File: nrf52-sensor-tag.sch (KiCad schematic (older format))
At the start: 16 parts, among them IC2 VEML6030, IC3 MS860702BA01-50, J3 Conn_01x07_Male, U1 MS88SF2

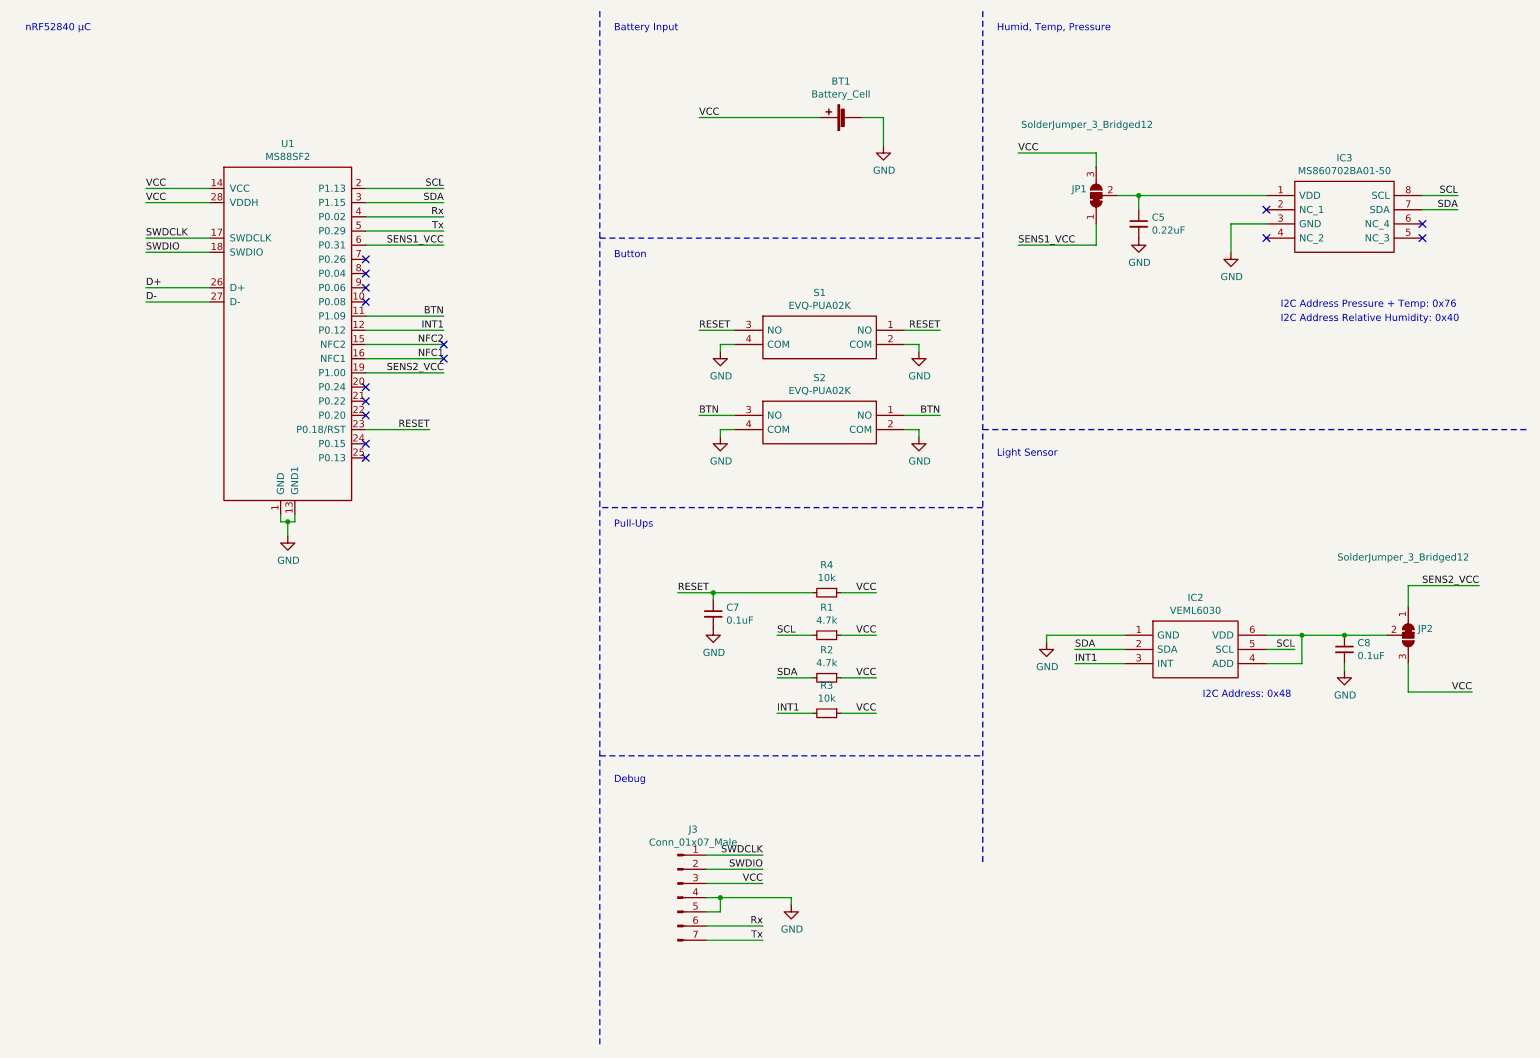
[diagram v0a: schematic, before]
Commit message: Add RGB LED
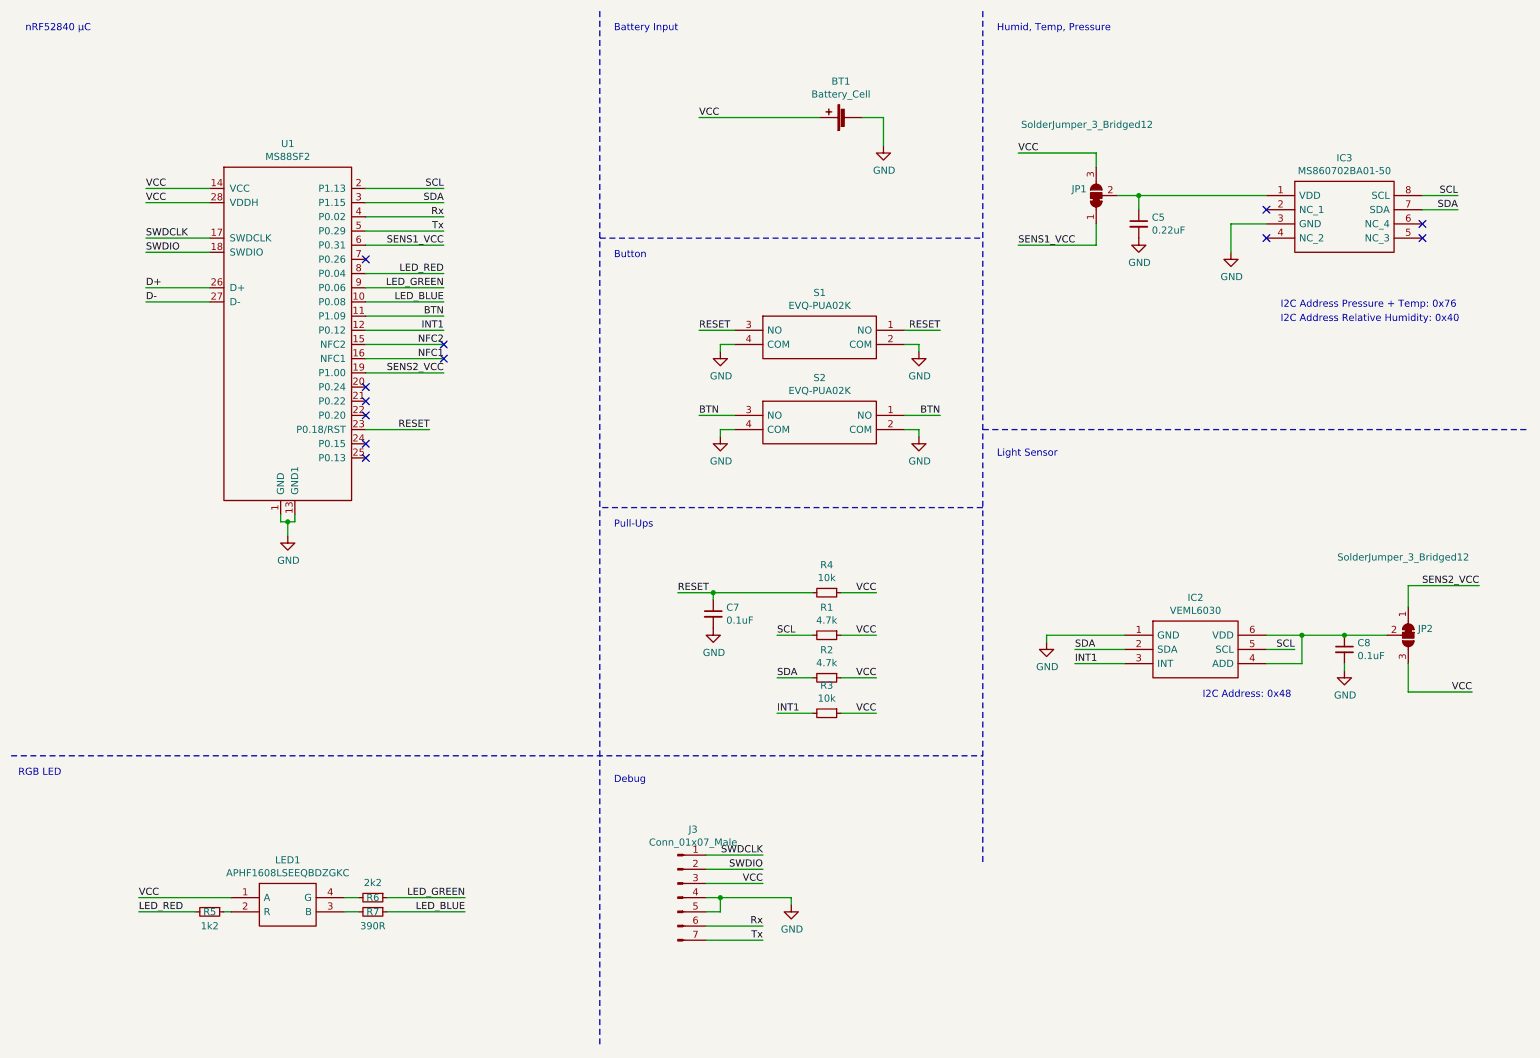
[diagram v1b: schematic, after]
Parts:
- added LED1: APHF1608LSEEQBDZGKC, APHF1608LSEEQBDZGKC:APHF1608LSEEQBDZGKC, symbol APHF1608LSEEQBDZGKC:APHF1608LSEEQBDZGKC
- added R5: 1k2, Resistor_SMD:R_0603_1608Metric, symbol Device:R_Small
- added R6: 2k2, Resistor_SMD:R_0603_1608Metric, symbol Device:R_Small
- added R7: 390R, Resistor_SMD:R_0603_1608Metric, symbol Device:R_Small
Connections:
- net VCC: now also LED1.1 (A)
- net LED_BLUE: now reaches U1.10 (P0.08)
- net LED_BLUE: now also R7.1
- net LED_RED: now reaches U1.8 (P0.04)
- net LED_RED: now also R5.2
- net LED_GREEN: now reaches U1.9 (P0.06)
- net LED_GREEN: now also R6.1
- new net: LED1.2 (R), R5.1
- new net: LED1.3 (B), R7.2
- new net: LED1.4 (G), R6.2
- no-connect marks 15 -> 12
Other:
- note added: "RGB LED"
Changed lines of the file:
@@
 	7350 4000 4650 4000
-Wire Notes Line
-	4650 5750 7350 5750
 Wire Notes Line
 	4650 500  4650 7800
@@
 Wire Wire Line
 	2450 4100 2500 4100
-NoConn ~ 3000 2550
 NoConn ~ 3000 3150
 NoConn ~ 3000 3250
@@
 Wire Wire Line
 	10350 5100 10350 5300
-NoConn ~ 3000 2450
-NoConn ~ 3000 2350
 NoConn ~ 3000 2250
 Wire Wire Line
@@
 Wire Wire Line
 	5350 1250 6200 1250
+$Comp
+L APHF1608LSEEQBDZGKC:APHF1608LSEEQBDZGKC LED1
+U 1 1 606A3F2A
+P 2050 6750
+F 0 "LED1" H 2450 7015 50  0000 C CNN
+F 1 "APHF1608LSEEQBDZGKC" H 2450 6924 50  0000 C CNN
+F 2 "APHF1608LSEEQBDZGKC:APHF1608LSEEQBDZGKC" H 2700 6850 50  0001 L CNN
+F 3 "https://componentsearchengine.com/Datasheets/1/APHF1608LSEEQBDZGKC.pdf" H 2700 6750 50  0001 L CNN
+F 4 "Standard LEDs - SMD RGB 0603 SMD" H 2700 6650 50  0001 L CNN "Description"
+F 5 "" H 2700 6550 50  0001 L CNN "Height"
+F 6 "Kingbright" H 2700 6450 50  0001 L CNN "Manufacturer_Name"
+F 7 "APHF1608LSEEQBDZGKC" H 2700 6350 50  0001 L CNN "Manufacturer_Part_Number"
+F 8 "604-APHF1608LQBDZGKC" H 2700 6250 50  0001 L CNN "Mouser Part Number"
+F 9 "https://www.mouser.co.uk/ProductDetail/Kingbright/APHF1608LSEEQBDZGKC?qs=YCa%2FAAYMW02iGkI4tWMQgA%3D%3D" H 2700 6150 50  0001 L CNN "Mouser Price/Stock"
+F 10 "APHF1608LSEEQBDZGKC" H 2700 6050 50  0001 L CNN "Arrow Part Number"
+F 11 "https://www.arrow.com/en/products/aphf1608lseeqbdzgkc/kingbright" H 2700 5950 50  0001 L CNN "Arrow Price/Stock"
+	1    2050 6750
+	1    0    0    -1
+$EndComp
+Text Label 1400 6750 0    50   ~ 0
+VCC
+$Comp
+L Device:R_Small R5
+U 1 1 606A6EBA
+P 1900 6850
+F 0 "R5" V 1900 6850 50  0000 C CNN
+F 1 "1k2" V 2000 6850 50  0000 C CNN
+F 2 "Resistor_SMD:R_0603_1608Metric" H 1900 6850 50  0001 C CNN
+F 3 "~" H 1900 6850 50  0001 C CNN
+	1    1900 6850
+	0    1    1    0
+$EndComp
+$Comp
+L Device:R_Small R6
+U 1 1 606A79B5
+P 3050 6750
+F 0 "R6" V 3050 6750 50  0000 C CNN
+F 1 "2k2" V 2945 6750 50  0000 C CNN
+F 2 "Resistor_SMD:R_0603_1608Metric" H 3050 6750 50  0001 C CNN
+F 3 "~" H 3050 6750 50  0001 C CNN
+	1    3050 6750
+	0    1    1    0
+$EndComp
+$Comp
+L Device:R_Small R7
+U 1 1 606A81A9
+P 3050 6850
+F 0 "R7" V 3050 6850 50  0000 C CNN
+F 1 "390R" V 3150 6850 50  0000 C CNN
+F 2 "Resistor_SMD:R_0603_1608Metric" H 3050 6850 50  0001 C CNN
+F 3 "~" H 3050 6850 50  0001 C CNN
+	1    3050 6850
+	0    1    1    0
+$EndComp
+Text Label 1400 6850 0    50   ~ 0
+LED_RED
+Text Label 3700 6750 2    50   ~ 0
+LED_GREEN
+Text Label 3700 6850 2    50   ~ 0
+LED_BLUE
+Wire Wire Line
+	3700 6750 3150 6750
+Wire Wire Line
+	3150 6850 3700 6850
+Wire Wire Line
+	2950 6850 2850 6850
+Wire Wire Line
+	2850 6750 2950 6750
+Wire Wire Line
+	2050 6850 2000 6850
+Wire Wire Line
+	1800 6850 1400 6850
+Wire Wire Line
+	1400 6750 2050 6750
+Wire Notes Line
+	500  5750 7350 5750
+Text Notes 550  5900 0    50   ~ 0
+RGB LED
+Text Label 3550 2350 2    50   ~ 0
+LED_RED
+Text Label 3550 2450 2    50   ~ 0
+LED_GREEN
+Text Label 3550 2550 2    50   ~ 0
+LED_BLUE
+Wire Wire Line
+	3000 2350 3550 2350
+Wire Wire Line
+	3550 2450 3000 2450
+Wire Wire Line
+	3000 2550 3550 2550
 $EndSCHEMATC

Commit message: #4 Sensor Tag improvements suggestions
https://github.com/HomeSmartMesh/nrf52_thread_sensortag/issues/4
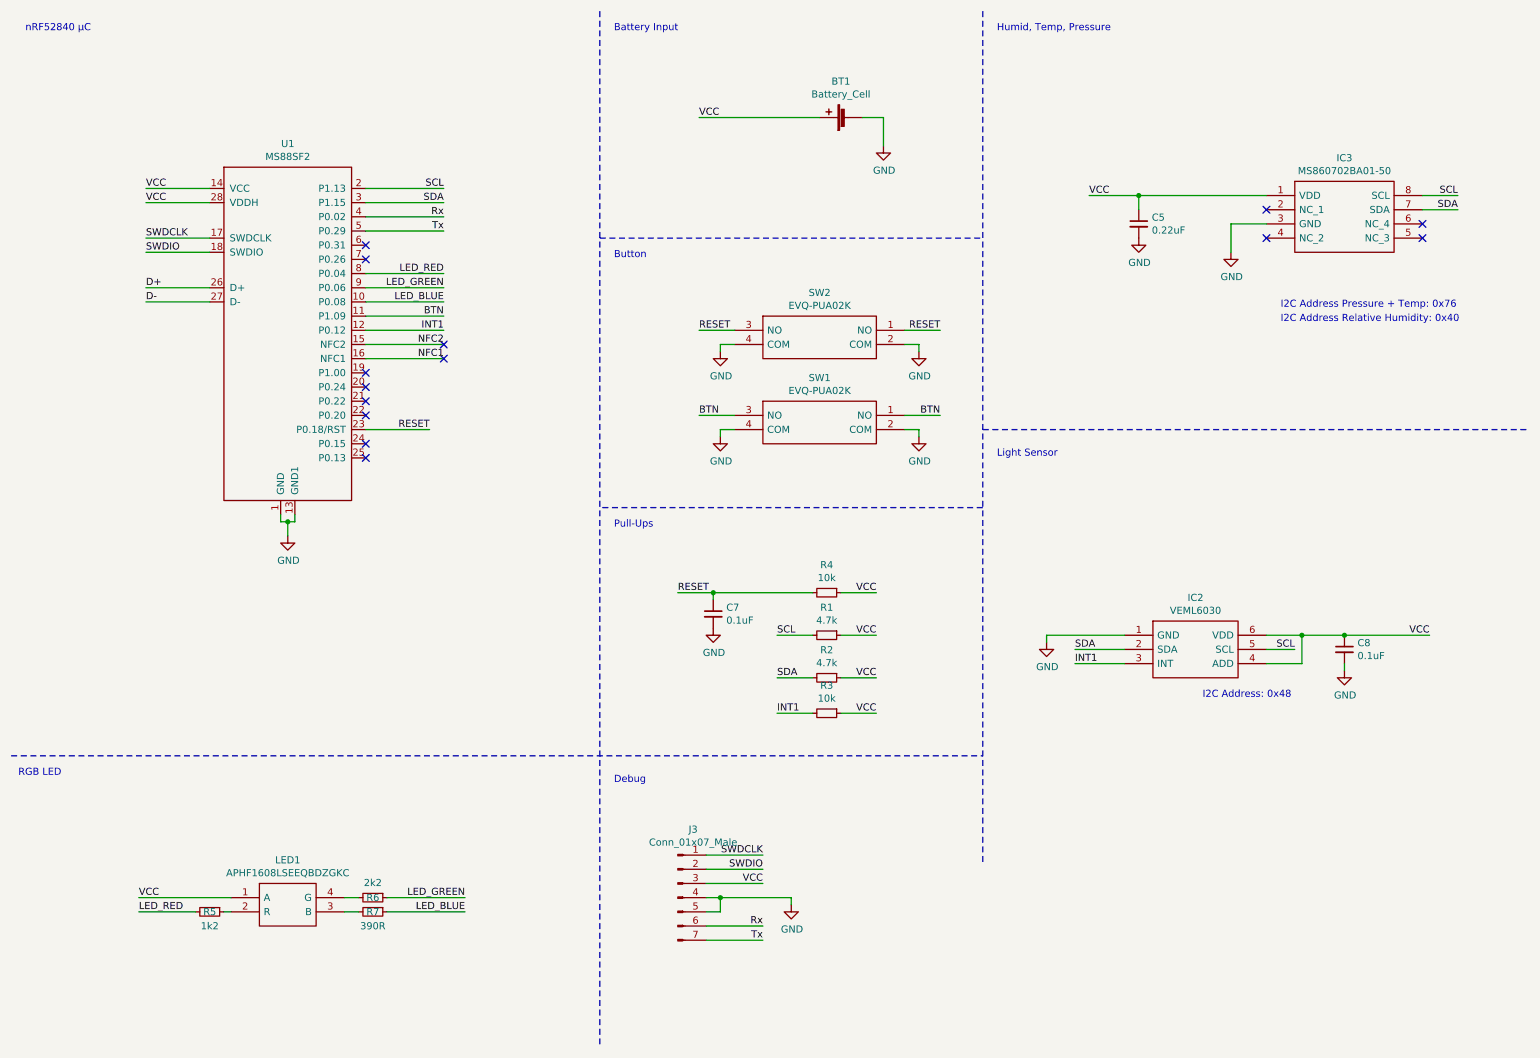
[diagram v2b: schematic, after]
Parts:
- removed JP1, JP2: SolderJumper_3_Bridged12, Jumper:SolderJumper-3_P1.3mm_Bridged12_RoundedPad1.0x1.5mm, symbol Jumper:SolderJumper_3_Bridged12
- renumbered S2 to SW1, S1 to SW2
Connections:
- net VCC: now also C5.1, C8.1, IC2.4 (ADD), IC2.6 (VDD), IC3.1 (VDD)
- net SENS1_VCC: no longer names the net of U1.6 (P0.31)
- net SENS2_VCC: no longer names the net of U1.19 (P1.00)
- no-connect marks 12 -> 14
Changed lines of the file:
@@
 Wire Wire Line
 	6600 4900 6350 4900
-Text Label 10850 4550 2    50   ~ 0
-SENS2_VCC
 Text Label 5900 5450 0    50   ~ 0
 INT1
@@
 INT1
 $Comp
-L EVQ-PUA02K:EVQ-PUA02K S1
+L EVQ-PUA02K:EVQ-PUA02K SW2
 U 1 1 602F21F2
 P 5600 2750
-F 0 "S1" H 6200 3015 50  0000 C CNN
+F 0 "SW2" H 6200 3015 50  0000 C CNN
 F 1 "EVQ-PUA02K" H 6200 2924 50  0000 C CNN
 F 2 "EVQ-PUA02K:EVQPUA02K" H 6650 2850 50  0001 L CNN
@@
 $EndComp
 $Comp
-L EVQ-PUA02K:EVQ-PUA02K S2
+L EVQ-PUA02K:EVQ-PUA02K SW1
 U 1 1 602F2ECF
 P 5600 3350
-F 0 "S2" H 6200 3615 50  0000 C CNN
+F 0 "SW1" H 6200 3615 50  0000 C CNN
 F 1 "EVQ-PUA02K" H 6200 3524 50  0000 C CNN
 F 2 "EVQ-PUA02K:EVQPUA02K" H 6650 3450 50  0001 L CNN
@@
 Wire Wire Line
 	5350 3350 5600 3350
-Text Label 3550 3050 2    50   ~ 0
-SENS2_VCC
-Text Label 3550 2150 2    50   ~ 0
-SENS1_VCC
-Wire Wire Line
-	3000 2150 3550 2150
-Wire Wire Line
-	3000 3050 3550 3050
-Text Label 10800 5300 2    50   ~ 0
+Text Label 10500 4900 2    50   ~ 0
 VCC
 Text Label 5800 6550 2    50   ~ 0
@@
 	9600 5100 9600 4900
 Connection ~ 9600 4900
-Text Label 7600 1500 0    50   ~ 0
-VCC
-Text Label 7600 2150 0    50   ~ 0
-SENS1_VCC
+Text Label 8100 1800 0    50   ~ 0
+VCC
 $Comp
 L MS860702BA01-50:MS860702BA01-50 IC3
@@
 $EndComp
 Wire Wire Line
-	8300 1800 8450 1800
-Wire Wire Line
 	8450 1900 8450 1800
 Connection ~ 8450 1800
@@
 NoConn ~ 3000 3550
 NoConn ~ 3000 3650
-$Comp
-L Jumper:SolderJumper_3_Bridged12 JP1
-U 1 1 603ADD74
-P 8150 1800
-F 0 "JP1" V 8196 1868 50  0000 L CNN
-F 1 "SolderJumper_3_Bridged12" V 8650 1400 50  0000 L CNN
-F 2 "Jumper:SolderJumper-3_P1.3mm_Bridged12_RoundedPad1.0x1.5mm" H 8150 1800 50  0001 C CNN
-F 3 "~" H 8150 1800 50  0001 C CNN
-	1    8150 1800
-	0    -1   -1   0
-$EndComp
-$Comp
-L Jumper:SolderJumper_3_Bridged12 JP2
-U 1 1 603AE514
-P 10350 4900
-F 0 "JP2" V 10304 4968 50  0000 L CNN
-F 1 "SolderJumper_3_Bridged12" V 9800 4400 50  0000 L CNN
-F 2 "Jumper:SolderJumper-3_P1.3mm_Bridged12_RoundedPad1.0x1.5mm" H 10350 4900 50  0001 C CNN
-F 3 "~" H 10350 4900 50  0001 C CNN
-	1    10350 4900
-	0    1    1    0
-$EndComp
-Wire Wire Line
-	7600 2150 8150 2150
-Wire Wire Line
-	8150 2150 8150 2000
-Wire Wire Line
-	8150 1600 8150 1500
-Wire Wire Line
-	8150 1500 7600 1500
-Wire Wire Line
-	10200 4900 9900 4900
-Wire Wire Line
-	10850 4550 10350 4550
-Wire Wire Line
-	10350 4550 10350 4700
-Wire Wire Line
-	10800 5300 10350 5300
-Wire Wire Line
-	10350 5100 10350 5300
 NoConn ~ 3000 2250
 Wire Wire Line
@@
 Wire Wire Line
 	3000 2550 3550 2550
+Wire Wire Line
+	8100 1800 8450 1800
+Wire Wire Line
+	9900 4900 10500 4900
+NoConn ~ 3000 2150
+NoConn ~ 3000 3050
 $EndSCHEMATC

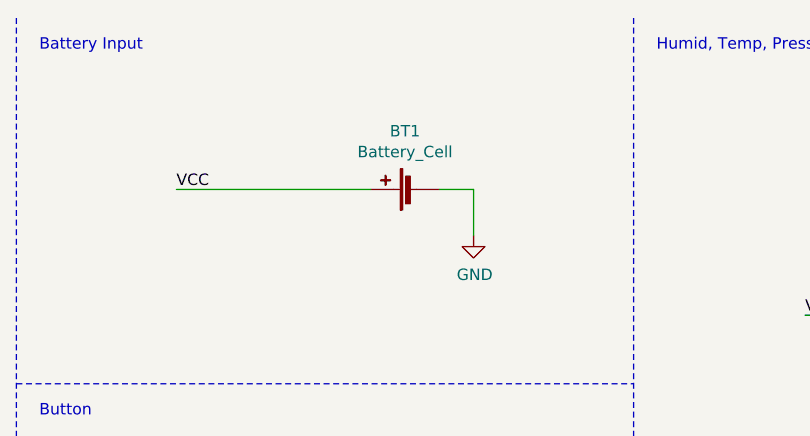
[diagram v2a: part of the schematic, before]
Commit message: Generated BOM and Gerbers for v1.1
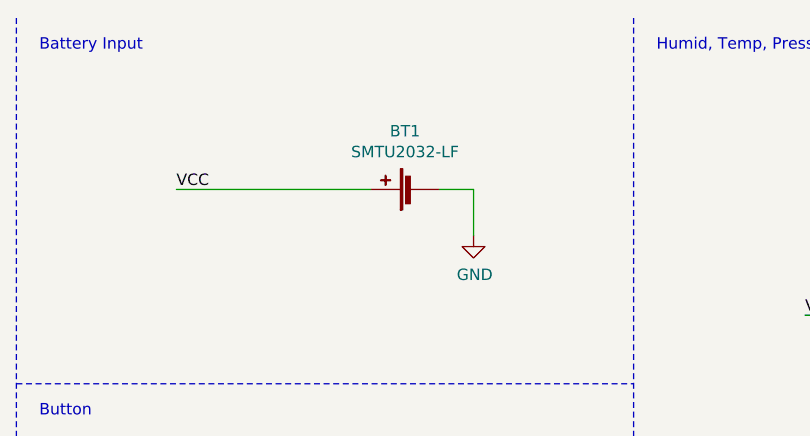
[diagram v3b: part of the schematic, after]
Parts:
- BT1: value Battery_Cell -> SMTU2032-LF
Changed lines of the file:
@@
 P 6400 1250
 F 0 "BT1" V 6655 1300 50  0000 C CNN
-F 1 "Battery_Cell" V 6564 1300 50  0000 C CNN
+F 1 "SMTU2032-LF" V 6564 1300 50  0000 C CNN
 F 2 "BA2032SM:BA2032SM" V 6400 1310 50  0001 C CNN
 F 3 "~" V 6400 1310 50  0001 C CNN

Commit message: Finalized schematics + generated manufacturing files
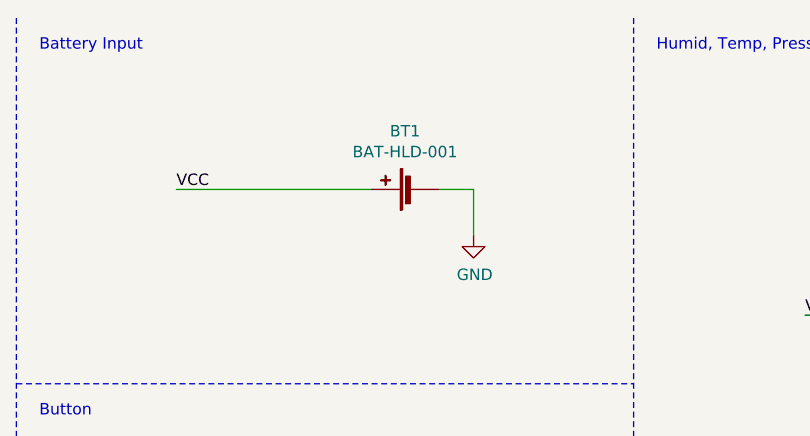
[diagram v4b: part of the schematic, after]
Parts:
- BT1: value SMTU2032-LF -> BAT-HLD-001; footprint BA2032SM:BA2032SM -> BAT-HLD-001:BATHLD001
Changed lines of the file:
@@
 P 6400 1250
 F 0 "BT1" V 6655 1300 50  0000 C CNN
-F 1 "SMTU2032-LF" V 6564 1300 50  0000 C CNN
-F 2 "BA2032SM:BA2032SM" V 6400 1310 50  0001 C CNN
+F 1 "BAT-HLD-001" V 6564 1300 50  0000 C CNN
+F 2 "BAT-HLD-001:BATHLD001" V 6400 1310 50  0001 C CNN
 F 3 "~" V 6400 1310 50  0001 C CNN
 	1    6400 1250

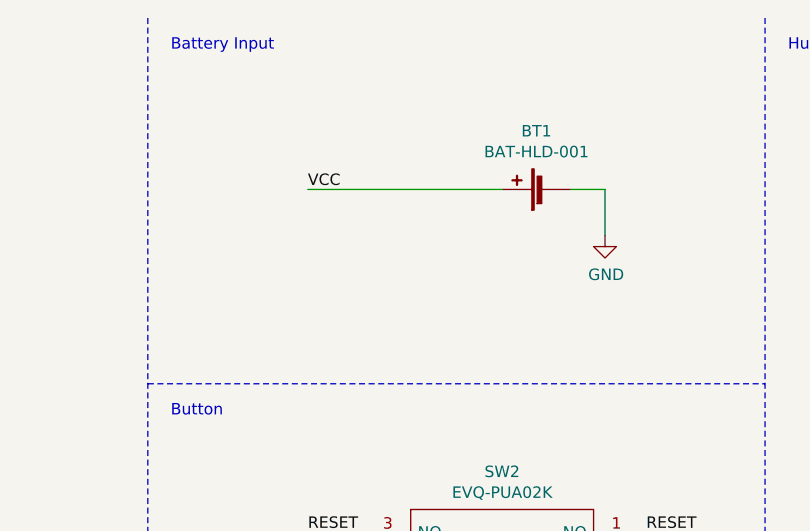
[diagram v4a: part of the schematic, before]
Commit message: Add 100uF cap + regenerated gerbers incl. F+B_Paste
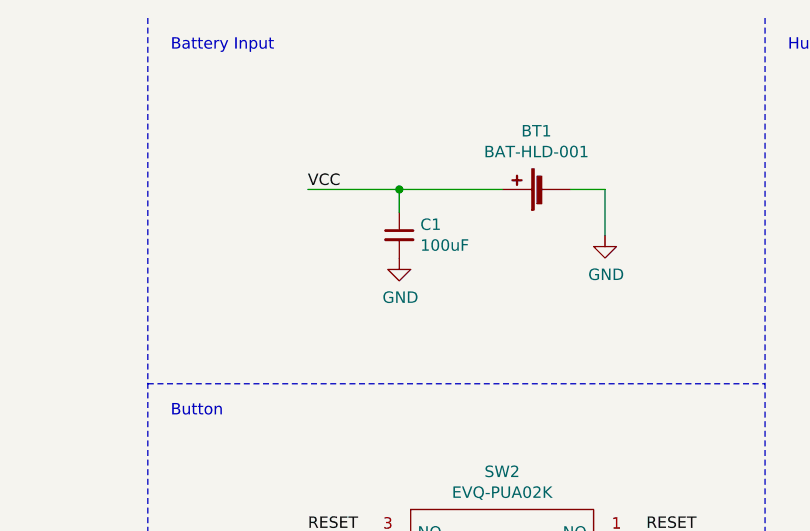
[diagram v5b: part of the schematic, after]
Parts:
- added C1: 100uF, Capacitor_SMD:C_1210_3225Metric, symbol Device:C_Small
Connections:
- net GND: now also C1.2
- net VCC: now also C1.1
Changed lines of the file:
@@
 Connection ~ 9900 4900
 Wire Wire Line
-	5350 1250 6200 1250
+	5350 1250 5750 1250
 $Comp
 L APHF1608LSEEQBDZGKC:APHF1608LSEEQBDZGKC LED1
@@
 NoConn ~ 3000 2150
 NoConn ~ 3000 3050
+$Comp
+L Device:C_Small C1
+U 1 1 612ED6EB
+P 5750 1450
+F 0 "C1" H 5842 1496 50  0000 L CNN
+F 1 "100uF" H 5842 1405 50  0000 L CNN
+F 2 "Capacitor_SMD:C_1210_3225Metric" H 5750 1450 50  0001 C CNN
+F 3 "~" H 5750 1450 50  0001 C CNN
+	1    5750 1450
+	1    0    0    -1
+$EndComp
+$Comp
+L power:GND #PWR0102
+U 1 1 612EE574
+P 5750 1550
+F 0 "#PWR0102" H 5750 1300 50  0001 C CNN
+F 1 "GND" H 5755 1377 50  0000 C CNN
+F 2 "" H 5750 1550 50  0001 C CNN
+F 3 "" H 5750 1550 50  0001 C CNN
+	1    5750 1550
+	1    0    0    -1
+$EndComp
+Wire Wire Line
+	5750 1350 5750 1250
+Connection ~ 5750 1250
+Wire Wire Line
+	5750 1250 6200 1250
 $EndSCHEMATC
